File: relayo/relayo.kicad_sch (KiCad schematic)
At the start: 34 parts, among them J1 24V, J2 Conn_01x02, J3 Conn_01x02, J4 Conn_01x02, J5 DB9_Female, Q1 TIP122, Q2 TIP122, Q3 TIP122, Q4 TIP122, U1 Buck

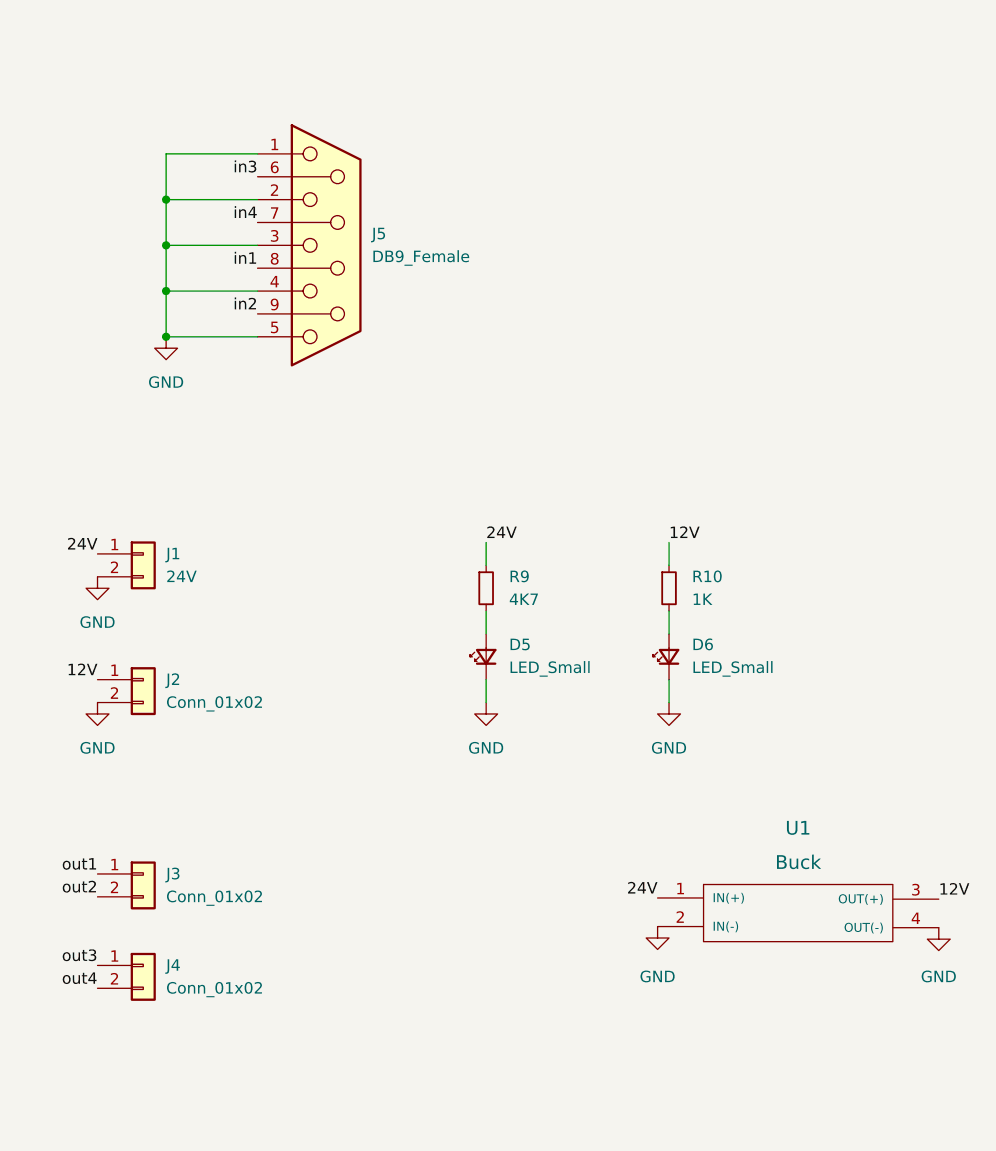
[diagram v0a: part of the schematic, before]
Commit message: Ckt Desgin done for 4 relay H bridge
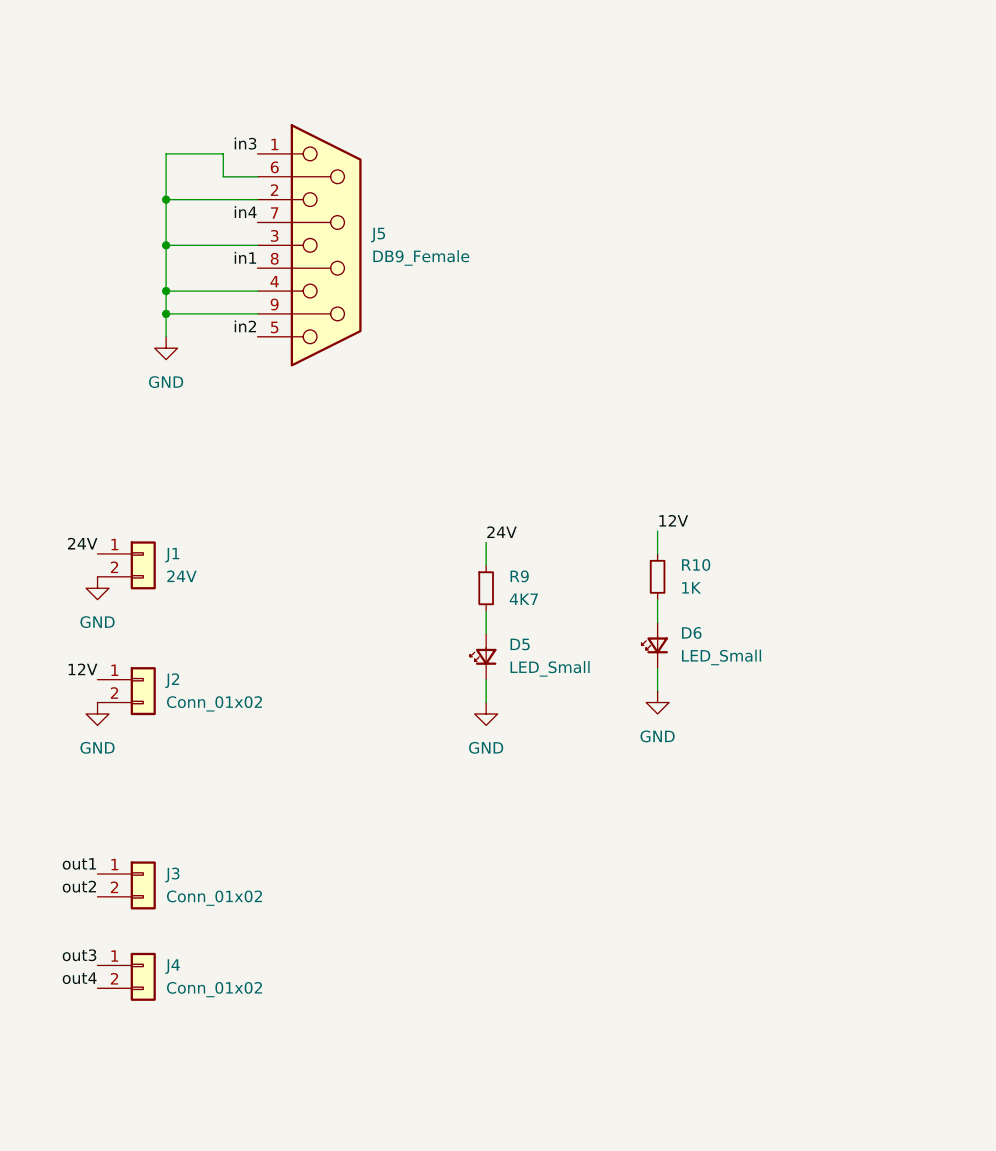
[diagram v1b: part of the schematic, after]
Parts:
- removed U1: Buck, modFiles:Buck 5A, symbol Prashant_library:Buck
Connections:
- net GND: now also J5.6, J5.9; no longer J5.1, J5.5
- net in2: now also J5.5; no longer J5.9
- net in3: now also J5.1; no longer J5.6

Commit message: Now Done
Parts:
- added H1, H2, H3, H4: MountingHole, MountingHole:MountingHole_4mm, symbol Mechanical:MountingHole
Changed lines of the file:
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@@
     (pin "2")
+  )
+  (symbol (lib_id "Mechanical:MountingHole") (at 223.52 130.81 0) (unit 1)
+    (in_bom yes) (on_board yes) (fields_autoplaced)
+    (property "Reference" "H4" (id 0) (at 226.06 129.5399 0)
+      (effects (font (size 1.27 1.27)) (justify left))
+    )
+    (property "Value" "MountingHole" (id 1) (at 226.06 132.0799 0)
+      (effects (font (size 1.27 1.27)) (justify left))
+    )
+    (property "Footprint" "MountingHole:MountingHole_4mm" (id 2) (at 223.52 130.81 0)
+      (effects (font (size 1.27 1.27)) hide)
+    )
+    (property "Datasheet" "~" (id 3) (at 223.52 130.81 0)
+      (effects (font (size 1.27 1.27)) hide)
+    )
   )
   (symbol (lib_id "power:GND") (at 31.75 133.35 0) (unit 1)
@@
     )
     (pin "1")
+  )
+  (symbol (lib_id "Mechanical:MountingHole") (at 223.52 107.95 0) (unit 1)
+    (in_bom yes) (on_board yes) (fields_autoplaced)
+    (property "Reference" "H1" (id 0) (at 226.06 106.6799 0)
+      (effects (font (size 1.27 1.27)) (justify left))
+    )
+    (property "Value" "MountingHole" (id 1) (at 226.06 109.2199 0)
+      (effects (font (size 1.27 1.27)) (justify left))
+    )
+    (property "Footprint" "MountingHole:MountingHole_4mm" (id 2) (at 223.52 107.95 0)
+      (effects (font (size 1.27 1.27)) hide)
+    )
+    (property "Datasheet" "~" (id 3) (at 223.52 107.95 0)
+      (effects (font (size 1.27 1.27)) hide)
+    )
   )
   (symbol (lib_id "power:GND") (at 57.15 93.98 180) (unit 1)
@@
     (pin "2")
   )
+  (symbol (lib_id "Mechanical:MountingHole") (at 223.52 115.57 0) (unit 1)
+    (in_bom yes) (on_board yes) (fields_autoplaced)
+    (property "Reference" "H2" (id 0) (at 226.06 114.2999 0)
+      (effects (font (size 1.27 1.27)) (justify left))
+    )
+    (property "Value" "MountingHole" (id 1) (at 226.06 116.8399 0)
+      (effects (font (size 1.27 1.27)) (justify left))
+    )
+    (property "Footprint" "MountingHole:MountingHole_4mm" (id 2) (at 223.52 115.57 0)
+      (effects (font (size 1.27 1.27)) hide)
+    )
+    (property "Datasheet" "~" (id 3) (at 223.52 115.57 0)
+      (effects (font (size 1.27 1.27)) hide)
+    )
+  )
   (symbol (lib_id "power:GND") (at 227.33 88.9 0) (unit 1)
     (in_bom yes) (on_board yes) (fields_autoplaced)
@@
     (pin "1")
   )
+  (symbol (lib_id "Mechanical:MountingHole") (at 223.52 123.19 0) (unit 1)
+    (in_bom yes) (on_board yes) (fields_autoplaced)
+    (property "Reference" "H3" (id 0) (at 226.06 121.9199 0)
+      (effects (font (size 1.27 1.27)) (justify left))
+    )
+    (property "Value" "MountingHole" (id 1) (at 226.06 124.4599 0)
+      (effects (font (size 1.27 1.27)) (justify left))
+    )
+    (property "Footprint" "MountingHole:MountingHole_4mm" (id 2) (at 223.52 123.19 0)
+      (effects (font (size 1.27 1.27)) hide)
+    )
+    (property "Datasheet" "~" (id 3) (at 223.52 123.19 0)
+      (effects (font (size 1.27 1.27)) hide)
+    )
+  )
   (sheet_instances
     (path "/" (page "1"))
@@
       (reference "F4") (unit 1) (value "Fuse") (footprint "modFiles:Fuse_Holder")
     )
+    (path "/276f198c-b311-46a9-bd98-d17d47ba3c1e"
+      (reference "H1") (unit 1) (value "MountingHole") (footprint "MountingHole:MountingHole_4mm")
+    )
+    (path "/8130bd0d-7237-434c-8bbf-d0816121fed4"
+      (reference "H2") (unit 1) (value "MountingHole") (footprint "MountingHole:MountingHole_4mm")
+    )
+    (path "/fd7a0ccf-cf00-4992-a9f4-c12eb28b4990"
+      (reference "H3") (unit 1) (value "MountingHole") (footprint "MountingHole:MountingHole_4mm")
+    )
+    (path "/1b8b1fac-76c3-46d7-b2d0-ad6f292d0c5f"
+      (reference "H4") (unit 1) (value "MountingHole") (footprint "MountingHole:MountingHole_4mm")
+    )
     (path "/bdc094ee-7c38-44c2-ab01-865762efe178"
